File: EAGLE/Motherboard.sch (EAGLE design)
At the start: 16 parts, among them T1 BC337

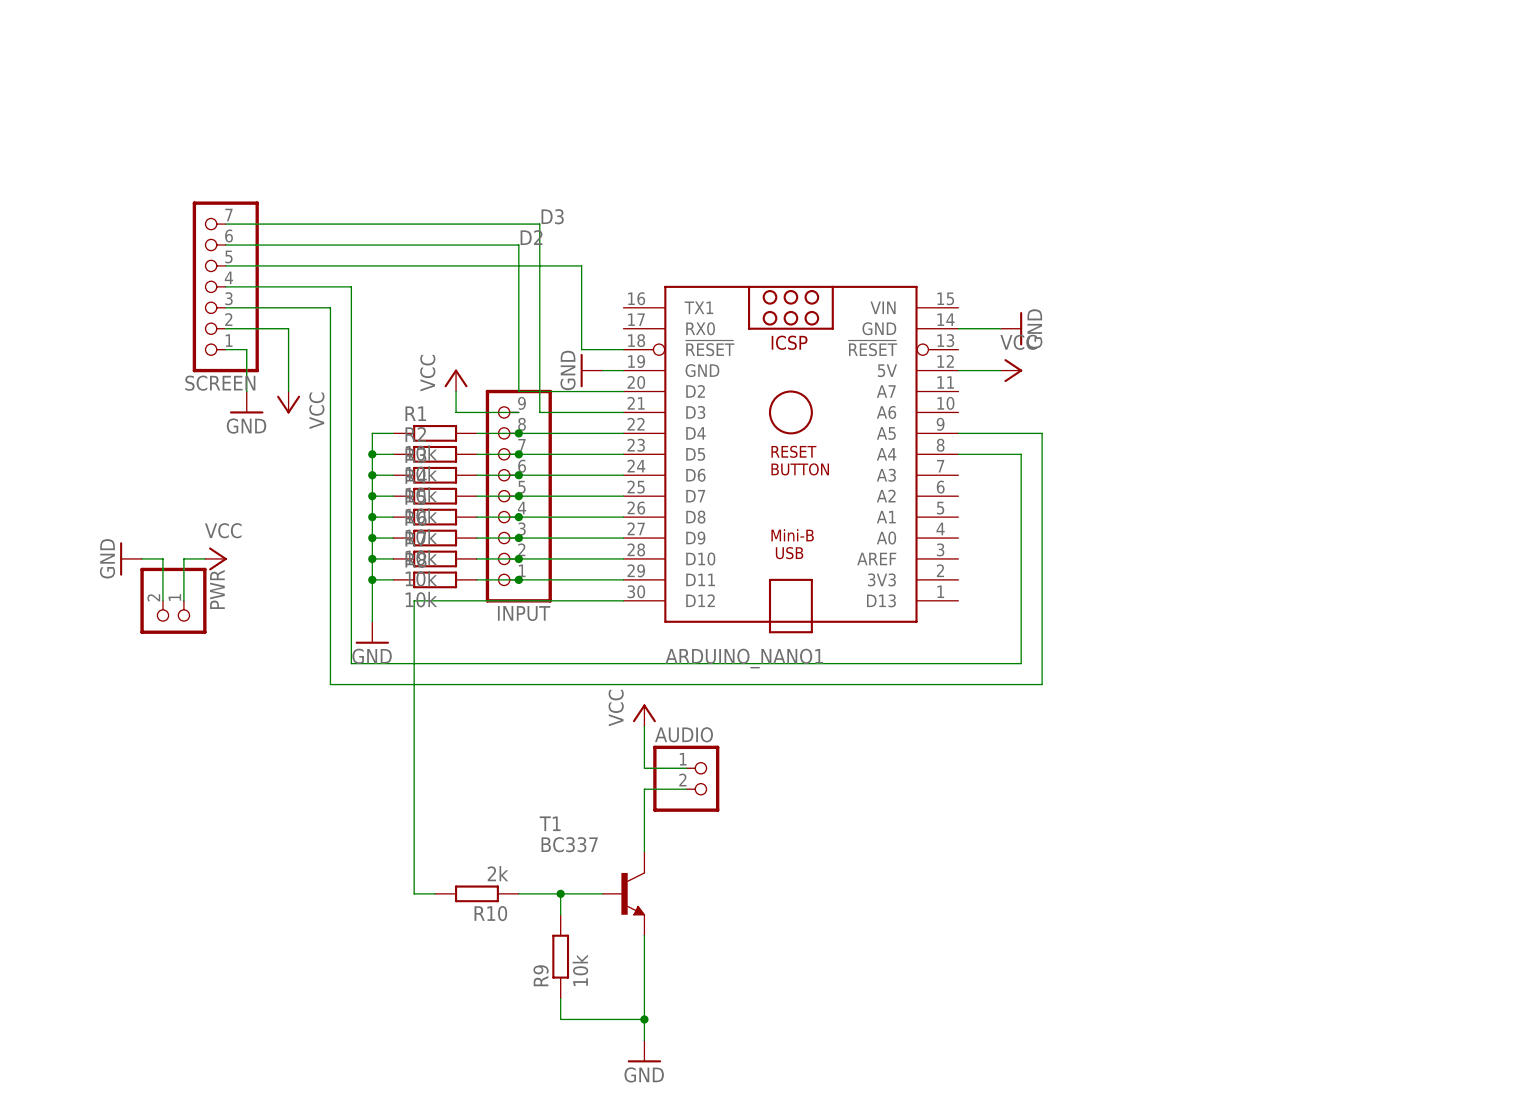
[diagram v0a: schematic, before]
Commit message: Updated EAGLE schematics and board
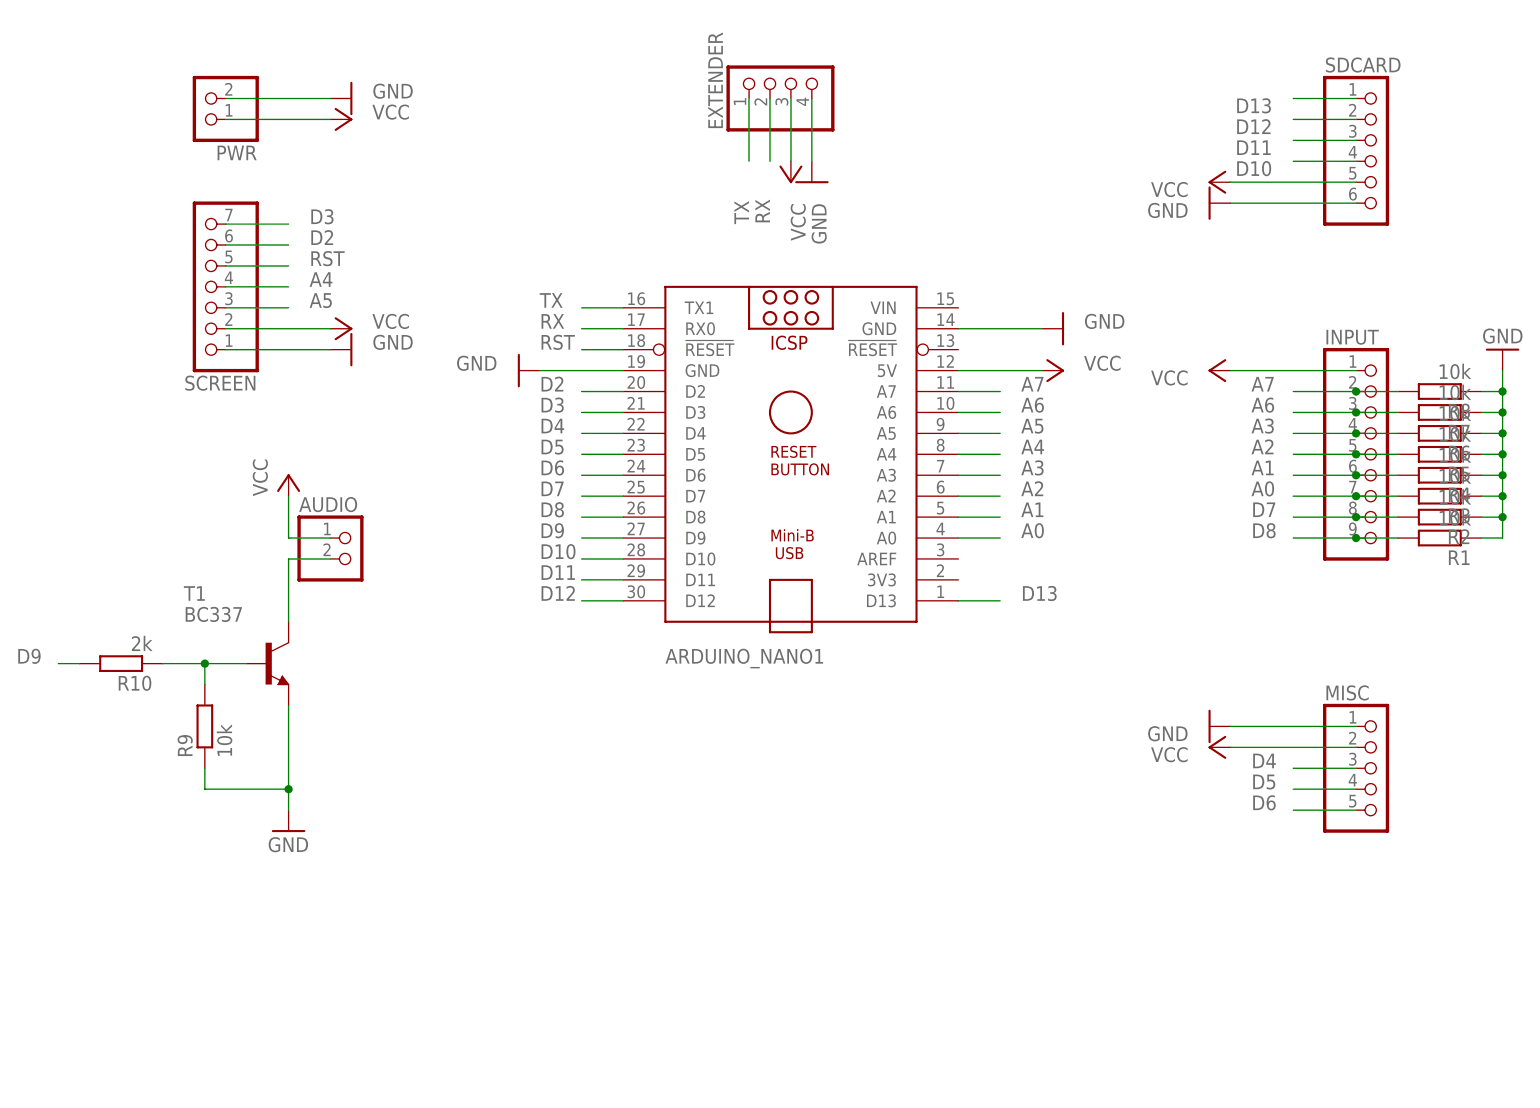
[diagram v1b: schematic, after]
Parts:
- added EXTENDER: (no value), pinhead:PINHD-1X4
- added MISC: (no value), pinhead:PINHD-1X5
- added SDCARD: (no value), pinhead:PINHD-1X6
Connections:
- net N$1 renamed A5
- net N$2 renamed A4
- net N$3 renamed RST
- removed net N$10: ARDUINO_NANO1.D10, INPUT.2, R7.2
- removed net N$11: ARDUINO_NANO1.D11, INPUT.1, R8.2
- removed net N$15: ARDUINO_NANO1.D12, R10.2
- removed net N$4: ARDUINO_NANO1.D4, INPUT.8, R1.2
- removed net N$5: ARDUINO_NANO1.D5, INPUT.7, R2.2
- removed net N$6: ARDUINO_NANO1.D6, INPUT.6, R3.2
- removed net N$7: ARDUINO_NANO1.D7, INPUT.5, R4.2
- removed net N$8: ARDUINO_NANO1.D8, INPUT.4, R5.2
- removed net N$9: ARDUINO_NANO1.D9, INPUT.3, R6.2
- new net A0: ARDUINO_NANO1.A0, INPUT.7, R3.2
- new net A1: ARDUINO_NANO1.A1, INPUT.6, R4.2
- new net A2: ARDUINO_NANO1.A2, INPUT.5, R5.2
- new net A3: ARDUINO_NANO1.A3, INPUT.4, R6.2
- new net A6: ARDUINO_NANO1.A6, INPUT.3, R7.2
- new net A7: ARDUINO_NANO1.A7, INPUT.2, R8.2
- new net D10: ARDUINO_NANO1.D10, SDCARD.4
- new net D11: ARDUINO_NANO1.D11, SDCARD.3
- new net D12: ARDUINO_NANO1.D12, SDCARD.2
- new net D13: ARDUINO_NANO1.D13, SDCARD.1
- new net D4: ARDUINO_NANO1.D4, MISC.3
- new net D5: ARDUINO_NANO1.D5, MISC.4
- new net D6: ARDUINO_NANO1.D6, MISC.5
- new net D7: ARDUINO_NANO1.D7, INPUT.8, R2.2
- new net D8: ARDUINO_NANO1.D8, INPUT.9, R1.2
- new net D9: ARDUINO_NANO1.D9, R10.2
- new net RX: ARDUINO_NANO1.RX0, EXTENDER.2
- new net TX: ARDUINO_NANO1.TX1, EXTENDER.1
- net GND: now also EXTENDER.4, MISC.1, SDCARD.6
- net VCC: now also EXTENDER.3, INPUT.1, MISC.2, SDCARD.5; no longer INPUT.9
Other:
- moved on the sheet: AUDIO, INPUT, PWR, R1, R10, R2, R3, R4, R5, R6, R7, R8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

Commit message: Updated motherboard schetch and board design
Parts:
- added C1, C2: (no value), rcl:CPOL-USE2.5-6
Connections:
- net GND: now also C1.-, C2.-
- net VCC: now also C1.+, C2.+
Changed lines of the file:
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@@
 <part name="GND9" library="supply1" library_urn="urn:adsk.eagle:library:371" deviceset="GND" device=""/>
 <part name="P+8" library="supply1" library_urn="urn:adsk.eagle:library:371" deviceset="VCC" device=""/>
+<part name="C1" library="rcl" library_urn="urn:adsk.eagle:library:334" deviceset="CPOL-US" device="E2.5-6" package3d_urn="urn:adsk.eagle:package:23349/1"/>
+<part name="C2" library="rcl" library_urn="urn:adsk.eagle:library:334" deviceset="CPOL-US" device="E2.5-6" package3d_urn="urn:adsk.eagle:package:23349/1"/>
+<part name="GND10" library="supply1" library_urn="urn:adsk.eagle:library:371" deviceset="GND" device=""/>
+<part name="GND11" library="supply1" library_urn="urn:adsk.eagle:library:371" deviceset="GND" device=""/>
+<part name="P+9" library="supply1" library_urn="urn:adsk.eagle:library:371" deviceset="VCC" device=""/>
+<part name="P+10" library="supply1" library_urn="urn:adsk.eagle:library:371" deviceset="VCC" device=""/>
 </parts>
 <sheets>
@@
 <instance part="P+8" gate="VCC" x="55.88" y="78.74" smashed="yes" rot="R180">
 <attribute name="VALUE" x="55.88" y="76.2" size="1.778" layer="96" rot="R270"/>
+</instance>
+<instance part="C1" gate="G$1" x="25.4" y="-5.08" smashed="yes">
+<attribute name="NAME" x="26.416" y="-4.445" size="1.778" layer="95"/>
+<attribute name="VALUE" x="26.416" y="-9.271" size="1.778" layer="96"/>
+</instance>
+<instance part="C2" gate="G$1" x="40.64" y="-5.08" smashed="yes">
+<attribute name="NAME" x="41.656" y="-4.445" size="1.778" layer="95"/>
+<attribute name="VALUE" x="41.656" y="-9.271" size="1.778" layer="96"/>
+</instance>
+<instance part="GND10" gate="1" x="25.4" y="-15.24" smashed="yes">
+<attribute name="VALUE" x="22.86" y="-17.78" size="1.778" layer="96"/>
+</instance>
+<instance part="GND11" gate="1" x="40.64" y="-15.24" smashed="yes">
+<attribute name="VALUE" x="38.1" y="-17.78" size="1.778" layer="96"/>
+</instance>
+<instance part="P+9" gate="VCC" x="25.4" y="2.54" smashed="yes">
+<attribute name="VALUE" x="22.86" y="0" size="1.778" layer="96" rot="R90"/>
+</instance>
+<instance part="P+10" gate="VCC" x="40.64" y="2.54" smashed="yes">
+<attribute name="VALUE" x="38.1" y="0" size="1.778" layer="96" rot="R90"/>
 </instance>
 </instances>
@@
 <wire x1="58.42" y1="81.28" x2="58.42" y2="88.9" width="0.1524" layer="91"/>
 </segment>
+<segment>
+<pinref part="GND10" gate="1" pin="GND"/>
+<pinref part="C1" gate="G$1" pin="-"/>
+<wire x1="25.4" y1="-12.7" x2="25.4" y2="-10.16" width="0.1524" layer="91"/>
+</segment>
+<segment>
+<pinref part="C2" gate="G$1" pin="-"/>
+<pinref part="GND11" gate="1" pin="GND"/>
+<wire x1="40.64" y1="-10.16" x2="40.64" y2="-12.7" width="0.1524" layer="91"/>
+</segment>
 </net>
 <net name="VCC" class="0">
@@
 <wire x1="55.88" y1="88.9" x2="55.88" y2="81.28" width="0.1524" layer="91"/>
 </segment>
+<segment>
+<pinref part="C1" gate="G$1" pin="+"/>
+<pinref part="P+9" gate="VCC" pin="VCC"/>
+<wire x1="25.4" y1="-2.54" x2="25.4" y2="0" width="0.1524" layer="91"/>
+</segment>
+<segment>
+<pinref part="P+10" gate="VCC" pin="VCC"/>
+<pinref part="C2" gate="G$1" pin="+"/>
+<wire x1="40.64" y1="0" x2="40.64" y2="-2.54" width="0.1524" layer="91"/>
+</segment>
 </net>

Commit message: * Redid the board design * Repinned a lot
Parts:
- MISC: device pinhead:PINHD-1X5 -> pinhead:PINHD-1X4
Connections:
- net A0: now also INPUT.9, R1.2; no longer INPUT.7, R3.2
- net A1: now also INPUT.8, R2.2; no longer INPUT.6, R4.2
- net A2: now also INPUT.7, R3.2; no longer INPUT.5, R5.2
- net A3: now also INPUT.6, R4.2; no longer INPUT.4, R6.2
- net A4: now also INPUT.5, R5.2; no longer SCREEN.4
- net A5: now also INPUT.4, R6.2; no longer SCREEN.3
- net D10: now also SDCARD.6; no longer SDCARD.4
- net D11: now also SCREEN.4, SDCARD.5; no longer SDCARD.3
- net D12: now also SDCARD.4; no longer SDCARD.2
- net D13: now also SCREEN.5, SDCARD.3; no longer SDCARD.1
- net D2: no longer SCREEN.6
- net D3: no longer SCREEN.7
- net D4: now also MISC.4; no longer MISC.3
- net D5: now also MISC.3; no longer MISC.4
- net D6: now also SCREEN.3; no longer MISC.5
- net D7: now also SCREEN.2; no longer INPUT.8, R2.2
- net D8: now also SCREEN.1; no longer INPUT.9, R1.2
- net GND: now also SCREEN.7, SDCARD.1; no longer SCREEN.1, SDCARD.6
- net RST: no longer SCREEN.5
- net VCC: now also SCREEN.6, SDCARD.2; no longer SCREEN.2, SDCARD.5
